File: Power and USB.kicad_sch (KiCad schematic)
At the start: 0 parts

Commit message: added sd card schematic and refactor page numbers and general tab
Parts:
- added J3: USB_C_Receptacle_USB2.0_16P, symbol Connector:USB_C_Receptacle_USB2.0_16P
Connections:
- new net: J3.A1 (GND), J3.A12 (GND), J3.B1 (GND), J3.B12 (GND)
- new net: J3.A4 (VBUS), J3.A9 (VBUS), J3.B4 (VBUS), J3.B9 (VBUS)
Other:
- title: (none) -> Interface - USB FS
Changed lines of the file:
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@@
 	(paper "A3")
 	(title_block
+		(title "Interface - USB FS")
 		(rev "${REVISION}")
 		(company "${COMPANY}")
 	)
+	(symbol
+		(lib_id "Connector:USB_C_Receptacle_USB2.0_16P")
+		(at 167.64 123.19 0)
+		(unit 1)
+		(exclude_from_sim no)
+		(in_bom yes)
+		(on_board yes)
+		(dnp no)
+		(fields_autoplaced yes)
+		(property "Reference" "J3"
+			(at 167.64 100.33 0)
+			(effects
+				(font
+					(size 1.27 1.27)
+				)
+			)
+		)
+		(property "Value" "USB_C_Receptacle_USB2.0_16P"
+			(at 167.64 102.87 0)
+			(effects
+				(font
+					(size 1.27 1.27)
+				)
+			)
+		)
+		(property "Footprint" ""
+			(at 171.45 123.19 0)
+			(effects
+				(font
+					(size 1.27 1.27)
+				)
+				(hide yes)
+			)
+		)
+		(property "Datasheet" "https://www.usb.org/sites/default/files/documents/usb_type-c.zip"
+			(at 171.45 123.19 0)
+			(effects
+				(font
+					(size 1.27 1.27)
+				)
+				(hide yes)
+			)
+		)
+		(property "Description" "USB 2.0-only 16P Type-C Receptacle connector"
+			(at 167.64 123.19 0)
+			(effects
+				(font
+					(size 1.27 1.27)
+				)
+				(hide yes)
+			)
+		)
+		(property "Supplier 1" ""
+			(at 167.64 123.19 0)
+			(effects
+				(font
+					(size 1.27 1.27)
+				)
+				(hide yes)
+			)
+		)
+		(property "Supplier Part Number 1" ""
+			(at 167.64 123.19 0)
+			(effects
+				(font
+					(size 1.27 1.27)
+				)
+				(hide yes)
+			)
+		)
+		(pin "A12"
+		)
+		(pin "B1"
+		)
+		(pin "B5"
+		)
+		(pin "A9"
+		)
+		(pin "B7"
+		)
+		(pin "B12"
+		)
+		(pin "S1"
+		)
+		(pin "A1"
+		)
+		(pin "B8"
+		)
+		(pin "B4"
+		)
+		(pin "A7"
+		)
+		(pin "B9"
+		)
+		(pin "B6"
+		)
+		(pin "A8"
+		)
+		(pin "A5"
+		)
+		(pin "A6"
+		)
+		(pin "A4"
+		)
+		(instances
+			(project ""
+				(path "/0650c7a8-acba-429c-9f8e-eec0baf0bc1c/fede4c36-00cc-4d3d-b71c-5243ba232202/97a2efac-bb12-4130-96cc-5d19fa63b112"
+					(reference "J3")
+					(unit 1)
+				)
+			)
+		)
+	)
 )

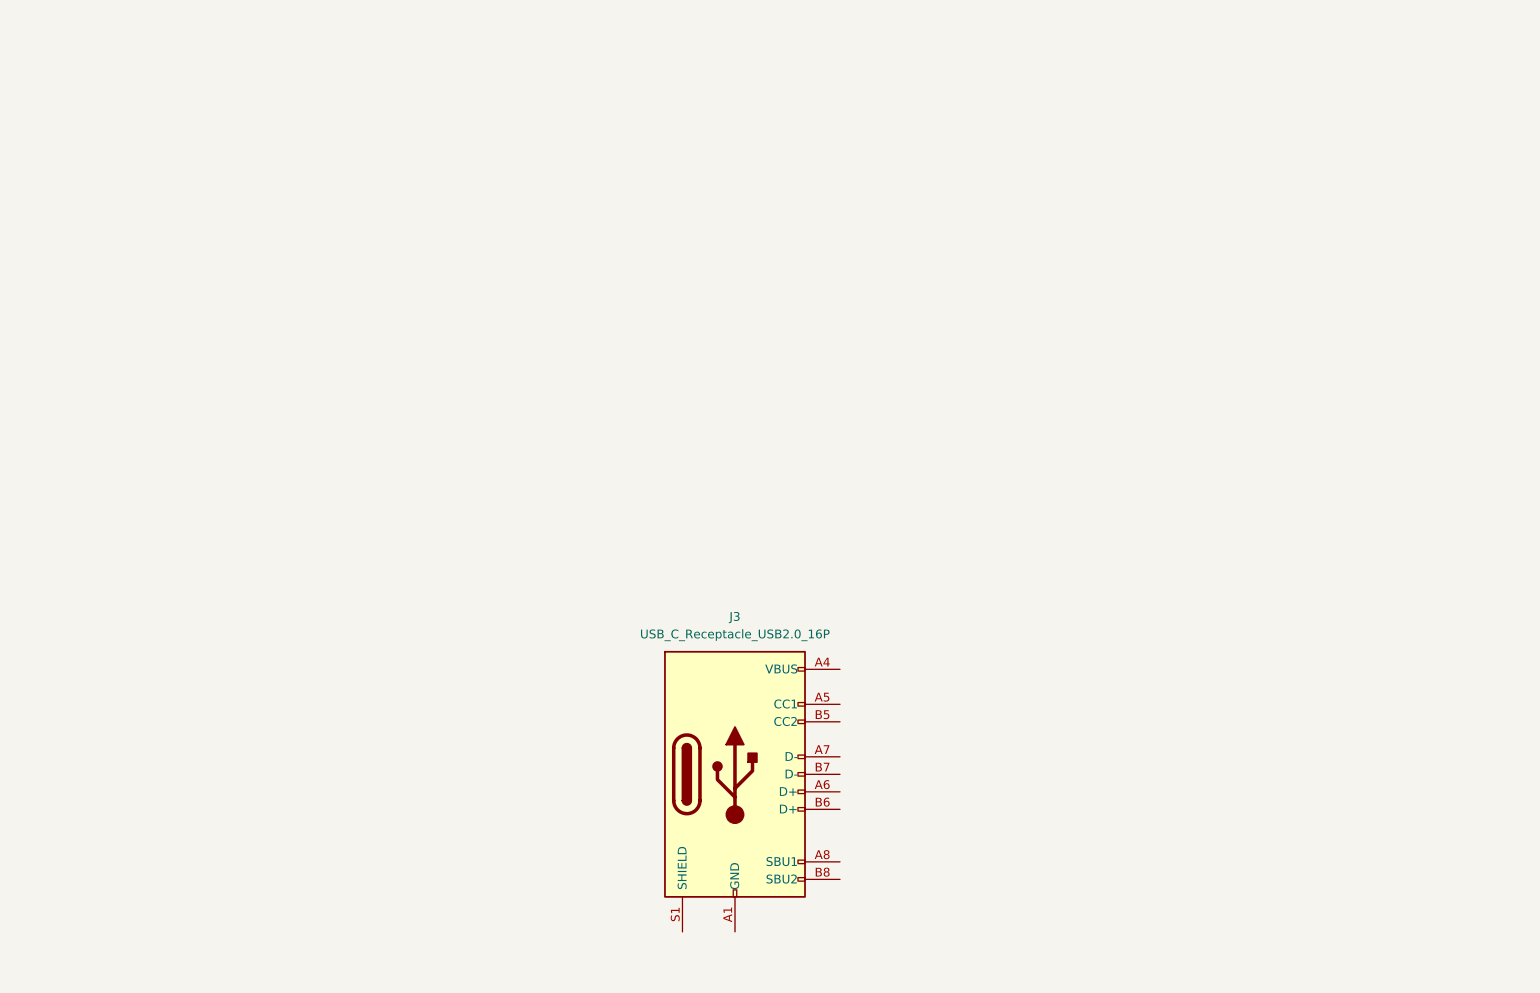
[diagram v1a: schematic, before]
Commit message: added emi for usb port and usb schematic
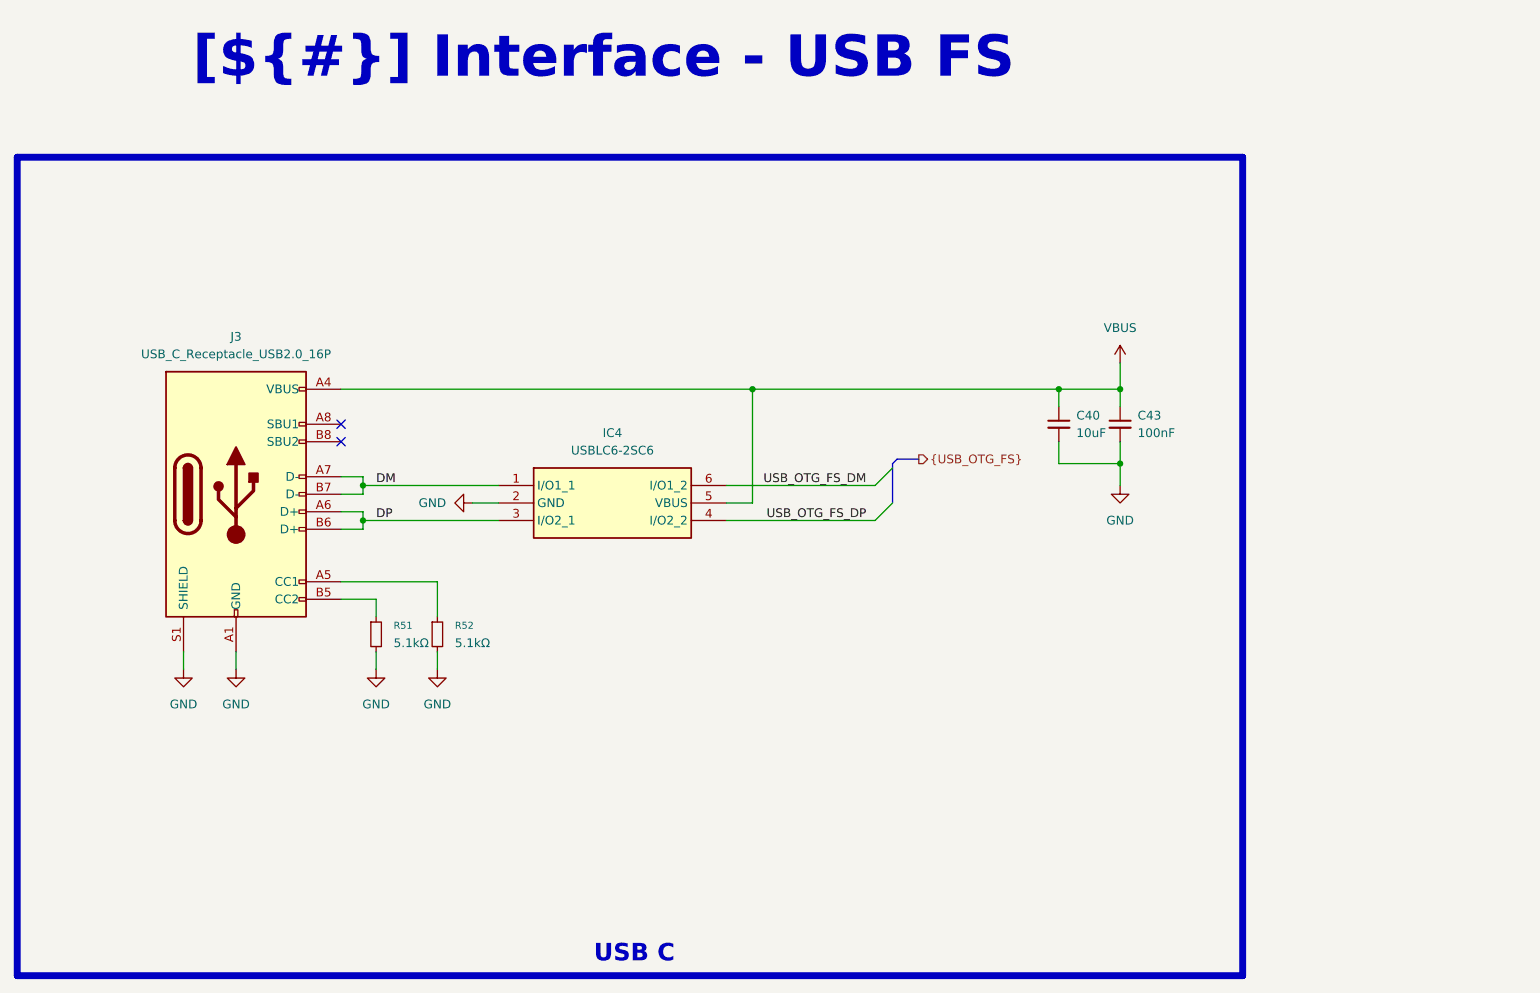
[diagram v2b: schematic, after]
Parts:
- added C40: 10uF, 0_capacitors:C_0805_2012Metric, symbol 0_capacitors:CL21A106KAYNNNE
- added C43: 100nF, 0_capacitors:C_0402_1005Metric, symbol 0_capacitors:CL05B104KO5NNNC
- added IC4: USBLC6-2SC6, 0_integrated_circuits:SOT95P280X145-6N, symbol 0_integrated_circuits:USBLC6-2SC6
- added R51, R52: 5.1kΩ, 0_resistors:R_0402_1005Metric, symbol 0_resistors:0402WGF5101TCE
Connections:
- net GND: now reaches J3.A1 (GND), J3.A12 (GND), J3.B1 (GND), J3.B12 (GND)
- net GND: now also J3.S1 (SHIELD), C40.2, C43.2, IC4.2 (GND), R51.2, R52.2
- net VBUS: now reaches J3.A4 (VBUS), J3.A9 (VBUS), J3.B4 (VBUS), J3.B9 (VBUS)
- net VBUS: now also C40.1, C43.1, IC4.5 (VBUS)
- net at J3.A5 (CC1): now also R52.1
- net DP: now reaches J3.A6 (D+)
- net DP: now also J3.B6 (D+), IC4.3 (I/O2_1)
- net DM: now reaches J3.A7 (D-)
- net DM: now also J3.B7 (D-), IC4.1 (I/O1_1)
- net at J3.B5 (CC2): now also R51.1
- new net USB_OTG_FS_DM: IC4.6 (I/O1_2)
- new net USB_OTG_FS_DP: IC4.4 (I/O2_2)
- no-connect marks 0 -> 2
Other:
- moved on the sheet: J3

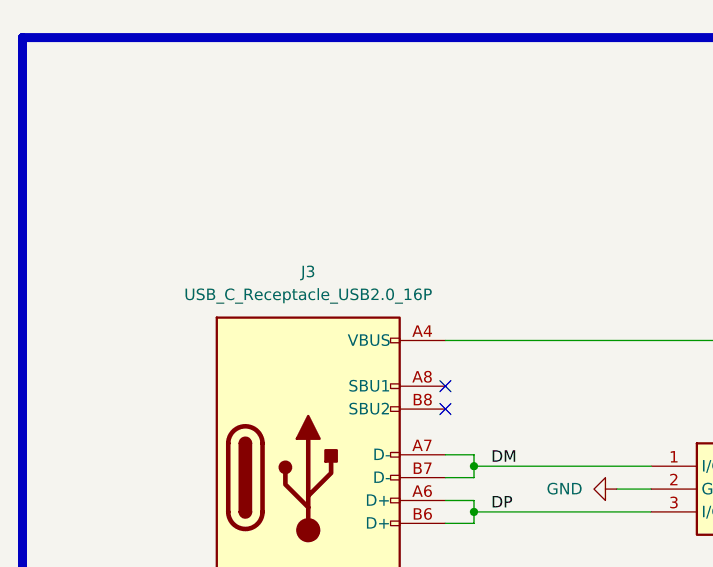
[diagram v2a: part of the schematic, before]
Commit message: usb new footprint
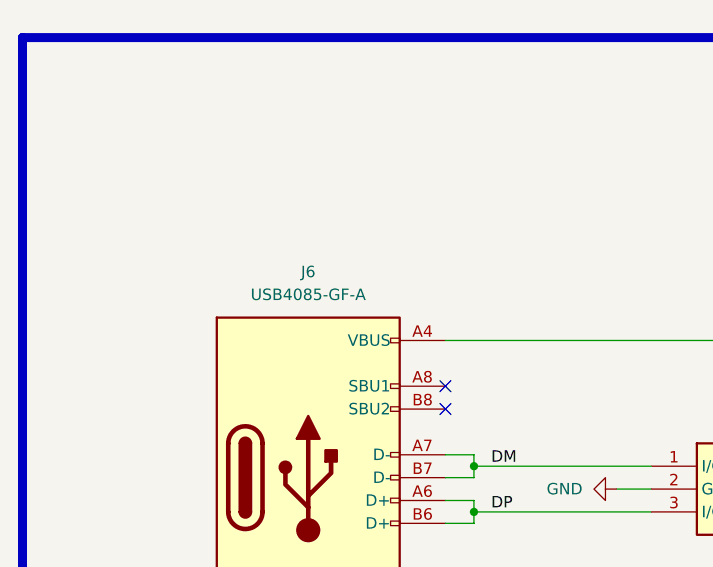
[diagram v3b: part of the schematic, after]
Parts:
- removed J3: USB_C_Receptacle_USB2.0_16P, symbol Connector:USB_C_Receptacle_USB2.0_16P
- added J6: USB4085-GF-A, 0_connectors:GCT_USB4085-GF-A_REVB, symbol 0_connectors:USB4085-GF-A
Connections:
- net DM: now also J6.A7 (D-), J6.B7 (D-)
- net DP: now also J6.A6 (D+), J6.B6 (D+)
- net GND: now also J6.A1 (GND), J6.A12 (GND), J6.B1 (GND), J6.B12 (GND), J6.S1 (SHIELD)
- net VBUS: now also J6.A4 (VBUS), J6.A9 (VBUS), J6.B4 (VBUS), J6.B9 (VBUS)
- net at R52.1: now also J6.A5 (CC1)
- net at R51.1: now also J6.B5 (CC2)
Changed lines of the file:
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@@
-	)
-	(symbol
-		(lib_id "Connector:USB_C_Receptacle_USB2.0_16P")
-		(at 95.25 82.55 0)
-		(unit 1)
-		(exclude_from_sim no)
-		(in_bom yes)
-		(on_board yes)
-		(dnp no)
-		(fields_autoplaced yes)
-		(property "Reference" "J3"
-			(at 95.25 59.69 0)
-			(effects
-				(font
-					(size 1.27 1.27)
-				)
-			)
-		)
-		(property "Value" "USB_C_Receptacle_USB2.0_16P"
-			(at 95.25 62.23 0)
-			(effects
-				(font
-					(size 1.27 1.27)
-				)
-			)
-		)
-		(property "Footprint" ""
-			(at 99.06 82.55 0)
-			(effects
-				(font
-					(size 1.27 1.27)
-				)
-				(hide yes)
-			)
-		)
-		(property "Datasheet" "https://www.usb.org/sites/default/files/documents/usb_type-c.zip"
-			(at 99.06 82.55 0)
-			(effects
-				(font
-					(size 1.27 1.27)
-				)
-				(hide yes)
-			)
-		)
-		(property "Description" "USB 2.0-only 16P Type-C Receptacle connector"
-			(at 95.25 82.55 0)
-			(effects
-				(font
-					(size 1.27 1.27)
-				)
-				(hide yes)
-			)
-		)
-		(property "Supplier 1" ""
-			(at 95.25 82.55 0)
-			(effects
-				(font
-					(size 1.27 1.27)
-				)
-				(hide yes)
-			)
-		)
-		(property "Supplier Part Number 1" ""
-			(at 95.25 82.55 0)
-			(effects
-				(font
-					(size 1.27 1.27)
-				)
-				(hide yes)
-			)
-		)
-		(pin "A12"
-		)
-		(pin "B1"
-		)
-		(pin "B5"
-		)
-		(pin "A9"
-		)
-		(pin "B7"
-		)
-		(pin "B12"
-		)
-		(pin "S1"
-		)
-		(pin "A1"
-		)
-		(pin "B8"
-		)
-		(pin "B4"
-		)
-		(pin "A7"
-		)
-		(pin "B9"
-		)
-		(pin "B6"
-		)
-		(pin "A8"
-		)
-		(pin "A5"
-		)
-		(pin "A6"
-		)
-		(pin "A4"
-		)
-		(instances
-			(project ""
-				(path "/0650c7a8-acba-429c-9f8e-eec0baf0bc1c/fede4c36-00cc-4d3d-b71c-5243ba232202/97a2efac-bb12-4130-96cc-5d19fa63b112"
-					(reference "J3")
-					(unit 1)
-				)
-			)
-		)
 	)
 	(symbol
@@
 					(unit 1)
 				)
+			)
+		)
+	)
+	(symbol
+		(lib_id "0_connectors:USB4085-GF-A")
+		(at 95.25 82.55 0)
+		(unit 1)
+		(exclude_from_sim no)
+		(in_bom yes)
+		(on_board yes)
+		(dnp no)
+		(fields_autoplaced yes)
+		(property "Reference" "J6"
+			(at 95.25 59.69 0)
+			(effects
+				(font
+					(size 1.27 1.27)
+				)
+			)
+		)
+		(property "Value" "USB4085-GF-A"
+			(at 95.25 62.23 0)
+			(effects
+				(font
+					(size 1.27 1.27)
+				)
+			)
+		)
+		(property "Footprint" "0_connectors:GCT_USB4085-GF-A_REVB"
+			(at 99.06 82.55 0)
+			(effects
+				(font
+					(size 1.27 1.27)
+				)
+				(hide yes)
+			)
+		)
+		(property "Datasheet" "USB4085-GF-A"
+			(at 99.06 82.55 0)
+			(effects
+				(font
+					(size 1.27 1.27)
+				)
+				(hide yes)
+			)
+		)
+		(property "Description" "USB 2.0-only 16P Type-C Receptacle connector"
+			(at 95.25 82.55 0)
+			(effects
+				(font
+					(size 1.27 1.27)
+				)
+				(hide yes)
+			)
+		)
+		(property "Supplier 1" "JLCPCB"
+			(at 95.25 82.55 0)
+			(effects
+				(font
+					(size 1.27 1.27)
+				)
+				(hide yes)
+			)
+		)
+		(property "Supplier Part Number 1" "C7095263"
+			(at 95.25 82.55 0)
+			(effects
+				(font
+					(size 1.27 1.27)
+				)
+				(hide yes)
+			)
+		)
+		(property "Supplier 2" "https://www.tme.eu/pl/details/usb4085-gf-a/zlacza-usb-i-ieee1394/gct/"
+			(at 95.25 82.55 0)
+			(effects
+				(font
+					(size 1.27 1.27)
+				)
+				(hide yes)
+			)
+		)
+		(pin "A6"
+		)
+		(pin "A12"
+		)
+		(pin "A4"
+		)
+		(pin "A7"
+		)
+		(pin "B8"
+		)
+		(pin "A5"
+		)
+		(pin "B5"
+		)
+		(pin "B1"
+		)
+		(pin "B4"
+		)
+		(pin "A1"
+		)
+		(pin "A9"
+		)
+		(pin "A8"
+		)
+		(pin "S1"
+		)
+		(pin "B9"
+		)
+		(pin "B12"
+		)
+		(pin "B7"
+		)
+		(pin "B6"
+		)
+		(instances
+			(project ""
+				(path "/0650c7a8-acba-429c-9f8e-eec0baf0bc1c/fede4c36-00cc-4d3d-b71c-5243ba232202/97a2efac-bb12-4130-96cc-5d19fa63b112"
+					(reference "J6")
+					(unit 1)
+				)

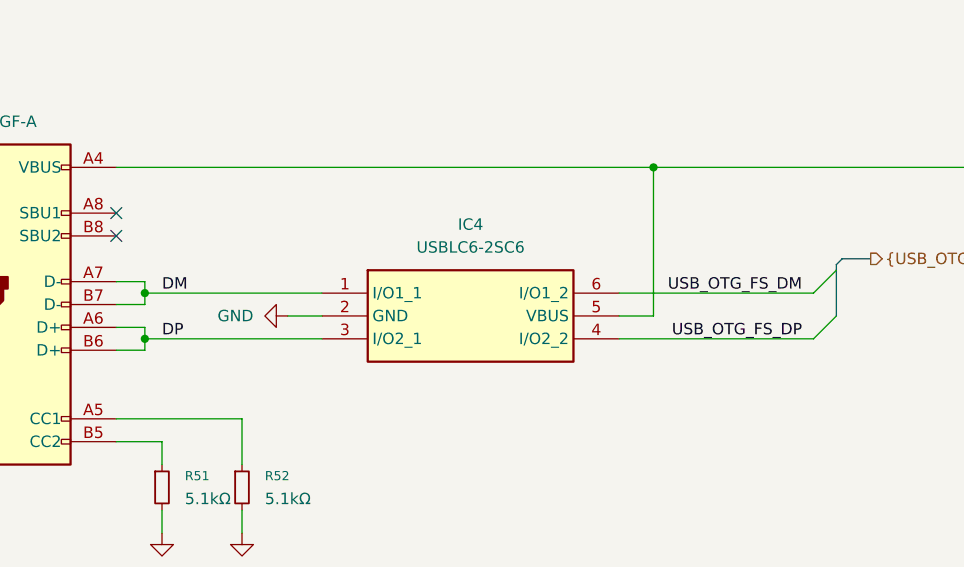
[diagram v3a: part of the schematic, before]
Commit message: duzo zmian, layout przetwornic i zasilania, wstepny routing sd card impedance control, usb differential impedance control
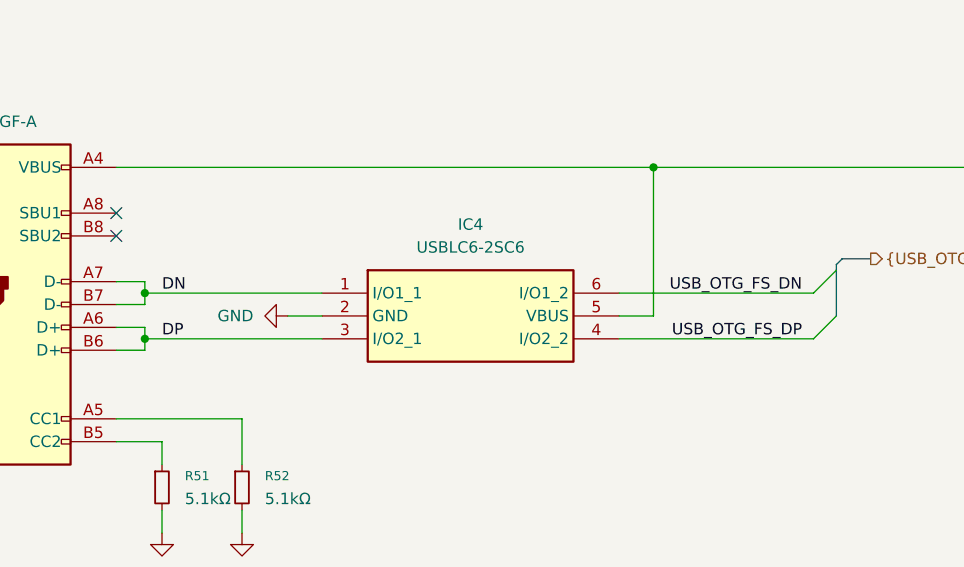
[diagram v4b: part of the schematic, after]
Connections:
- net DM renamed DN
- net USB_OTG_FS_DM renamed USB_OTG_FS_DN
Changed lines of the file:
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@@
 		)
 	)
-	(label "USB_OTG_FS_DM"
+	(label "USB_OTG_FS_DN"
 		(at 186.69 81.28 180)
 		(effects
@@
 		)
 	)
-	(label "DM"
+	(label "DN"
 		(at 115.57 81.28 0)
 		(effects
